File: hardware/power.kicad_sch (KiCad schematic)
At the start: 39 parts, among them J1 USB4110-GF-A, J2 B2B-PH-K-S, J3 PRPC001DAAN-RC, J4 PRPC001DAAN-RC, J5 PRPC001DAAN-RC, Q1 IRLML2246TRPBF, U1 USBLC6-2SC6, U2 BQ24074RGT, U3 TLV76733DGNR

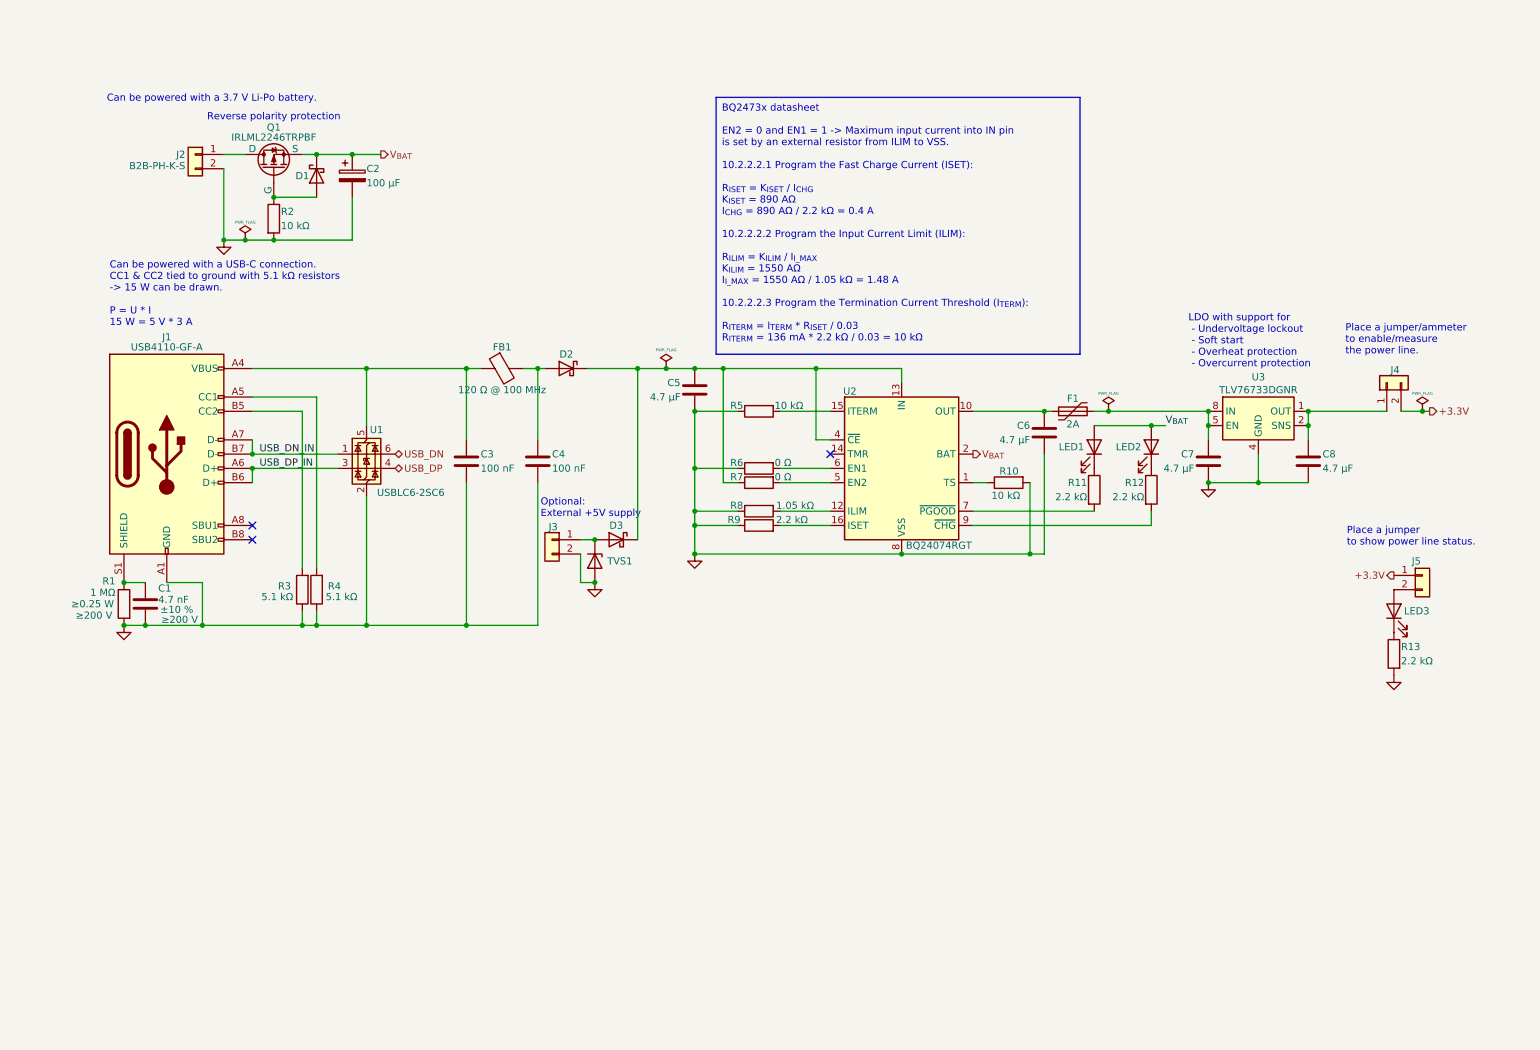
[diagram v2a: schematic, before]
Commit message: HW: Update components, change footprints to handsolder versions, finish power
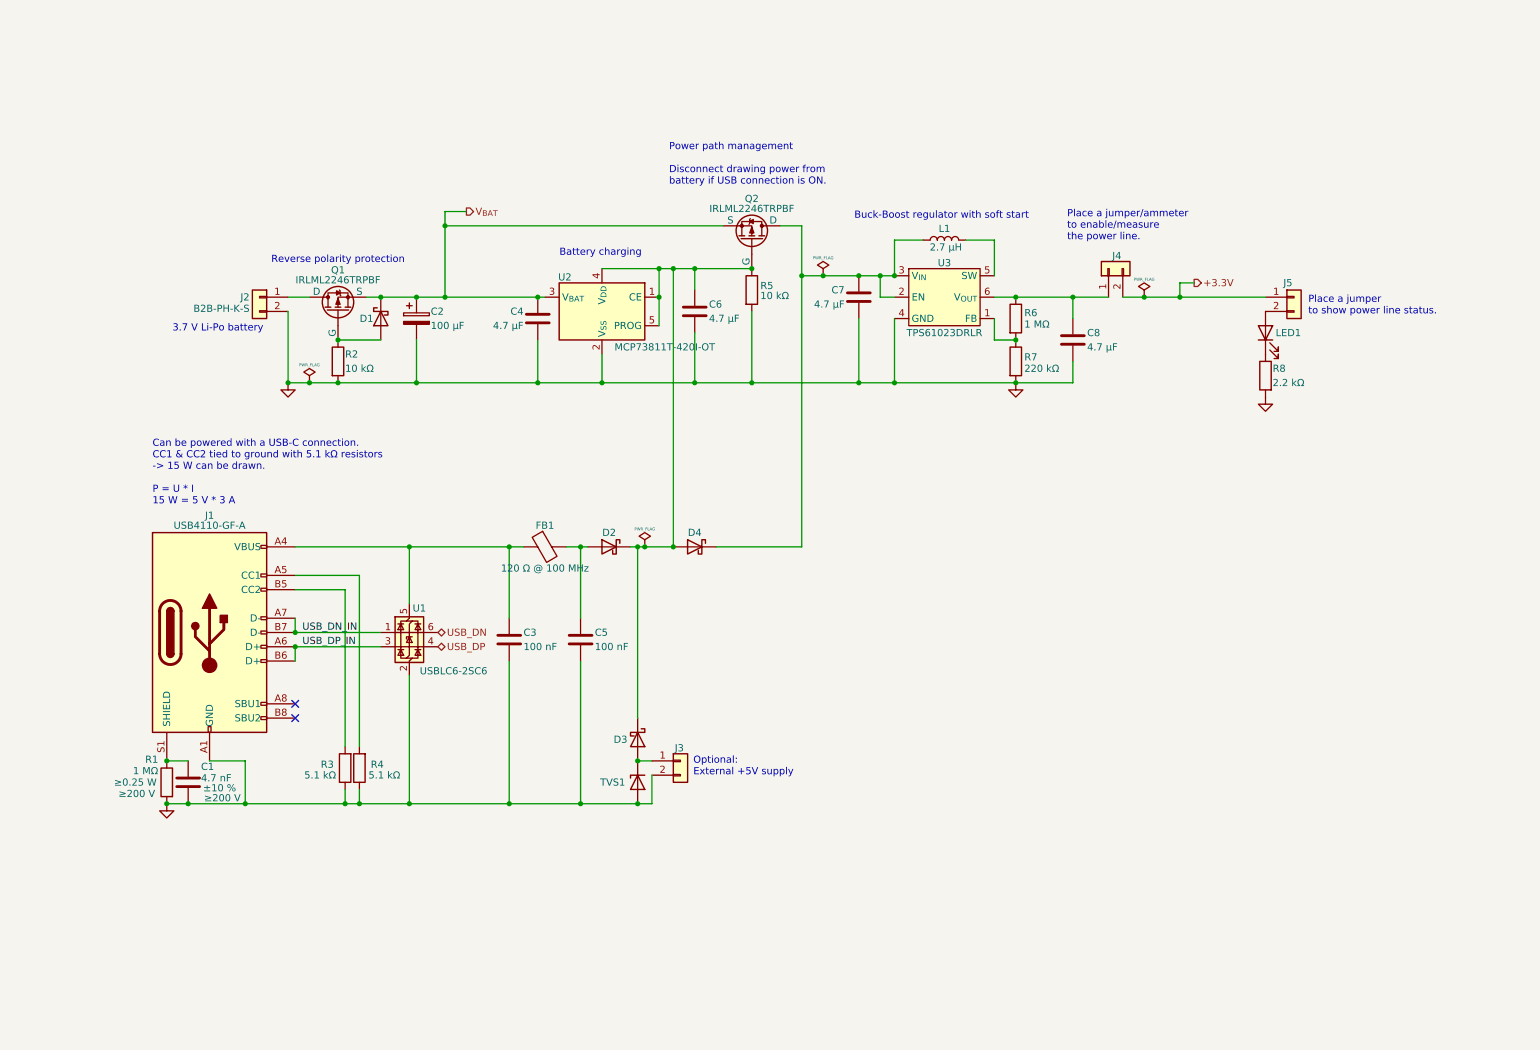
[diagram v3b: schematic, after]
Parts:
- removed C5: 4.7 µF, Capacitor_SMD:C_0603_1608Metric_Pad1.08x0.95mm_HandSolder, symbol Device:C
- removed F1: 2A, Fuse:Fuse_0805_2012Metric_Pad1.15x1.40mm_HandSolder, symbol Device:Polyfuse
- removed LED1, LED2: 150141YS73100, LED_SMD:LED_PLCC_2835_Handsoldering, symbol Device:LED
- removed R10: 10 kΩ, Resistor_SMD:R_0402_1005Metric_Pad0.72x0.64mm_HandSolder, symbol Device:R
- removed R11, R12, R9: 2.2 kΩ, Resistor_SMD:R_0402_1005Metric_Pad0.72x0.64mm_HandSolder, symbol Device:R
- removed R8: 1.05 kΩ, Resistor_SMD:R_0402_1005Metric_Pad0.72x0.64mm_HandSolder, symbol Device:R
- removed U2: BQ24074RGT, Package_DFN_QFN:VQFN-16-1EP_3x3mm_P0.5mm_EP1.68x1.68mm, symbol Battery_Management:BQ24074RGT
- removed U3: TLV76733DGNR, Package_SO:MSOP-8-1EP_3x3mm_P0.65mm_EP1.95x2.15mm, symbol TLV76733DGNR:TLV76733DGNR
- added C4: 4.7 µF, Capacitor_SMD:C_0603_1608Metric_Pad1.08x0.95mm_HandSolder, symbol Device:C
- added D4: CDBA140LL-HF, Diode_SMD:D_SMA_Handsoldering, symbol Device:D_Schottky
- added L1: 2.7 µH, Inductor_SMD:L_Bourns-SRU8028_8.0x8.0mm, symbol Device:L
- added Q2: IRLML2246TRPBF, Package_TO_SOT_SMD:SC-59_Handsoldering, symbol Simulation_SPICE:PMOS
- added U2: MCP73811T-420I-OT, Package_TO_SOT_SMD:SOT-23-5_HandSoldering, symbol Battery_Management:MCP73811T-420I-OT
- added U3: TPS61023DRLR, Package_TO_SOT_SMD:SOT-563, symbol TPS61023DRL:TPS61023DRLR
- R2, R5: Digi-Key Part Number 311-10.0KLRCT-ND -> 732-560112110020CT-ND; Manufacturer YAGEO -> Würth Elektronik; Manufacturer Part Number RC0402FR-0710KL -> 560112110020
- R3, R4: footprint Resistor_SMD:R_0402_1005Metric_Pad0.72x0.64mm_HandSolder -> Resistor_SMD:R_0603_1608Metric_Pad0.98x0.95mm_HandSolder; Digi-Key Part Number 311-5.10KLRCT-ND -> 732-560112120019CT-ND; Manufacturer YAGEO -> Würth Elektronik; Manufacturer Part Number RC0402FR-075K1L -> 560112120019
- R6: value 0 Ω -> 1 MΩ; footprint Resistor_SMD:R_0402_1005Metric_Pad0.72x0.64mm_HandSolder -> Resistor_SMD:R_1206_3216Metric_Pad1.30x1.75mm_HandSolder; Digi-Key Part Number 311-0.0JRCT-ND -> 732-560112132011CT-ND; Manufacturer YAGEO -> Würth Elektronik; Manufacturer Part Number RC0402JR-070RL -> 560112132011
- R7: value 0 Ω -> 220 kΩ; Digi-Key Part Number 311-0.0JRCT-ND -> 732-560112110217CT-ND; Manufacturer YAGEO -> Würth Elektronik; Manufacturer Part Number RC0402JR-070RL -> 560112110217
- R8: renamed from R13; Digi-Key Part Number 311-2.20KLRCT-ND -> 732-560112110087CT-ND; Manufacturer YAGEO -> Würth Elektronik; Manufacturer Part Number RC0402FR-072K2L -> 560112110087
- renumbered C4 to C5, LED3 to LED1
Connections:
- net GND: now also R5.2, R7.2, C4.2, U2.2 (V_{SS}), U3.4 (GND); no longer R5.1, R6.1
- net V_{BAT}: now also C4.1, Q2.3 (S), U2.3 (V_{BAT})
- net at C8.1, J4.1 (Pin_1): now also R6.1, U3.6 (V_{OUT})
- net at R6.2: now also R7.1, U3.1 (FB)
- net at C6.1: now also D2.1 (K), D3.1 (K), R5.1, D4.2 (A), Q2.2 (G), U2.1 (CE), U2.4 (V_{DD}), U2.5 (PROG)
- net at C7.1: now also D4.1 (K), L1.1, Q2.1 (D), U3.2 (EN), U3.3 (V_{IN})
- new net: L1.2, U3.5 (SW)
- no-connect marks 3 -> 2
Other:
- note added: "3.7 V Li-Po battery"
- note added: "Battery charging"
- note added: "Buck-Boost regulator with soft start"
- note added: "Power path management Disconnect drawing power from battery if USB connection is ON."
- note removed: "Can be powered with a 3.7 V Li-Po battery."
- note removed: "LDO with support for - Undervoltage lockout - Soft start - Overheat protection - Overcurrent protection"
- moved on the sheet: C1, C2, C3, C5, D1, D2, D3, FB1, J1, J2, J3, J4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

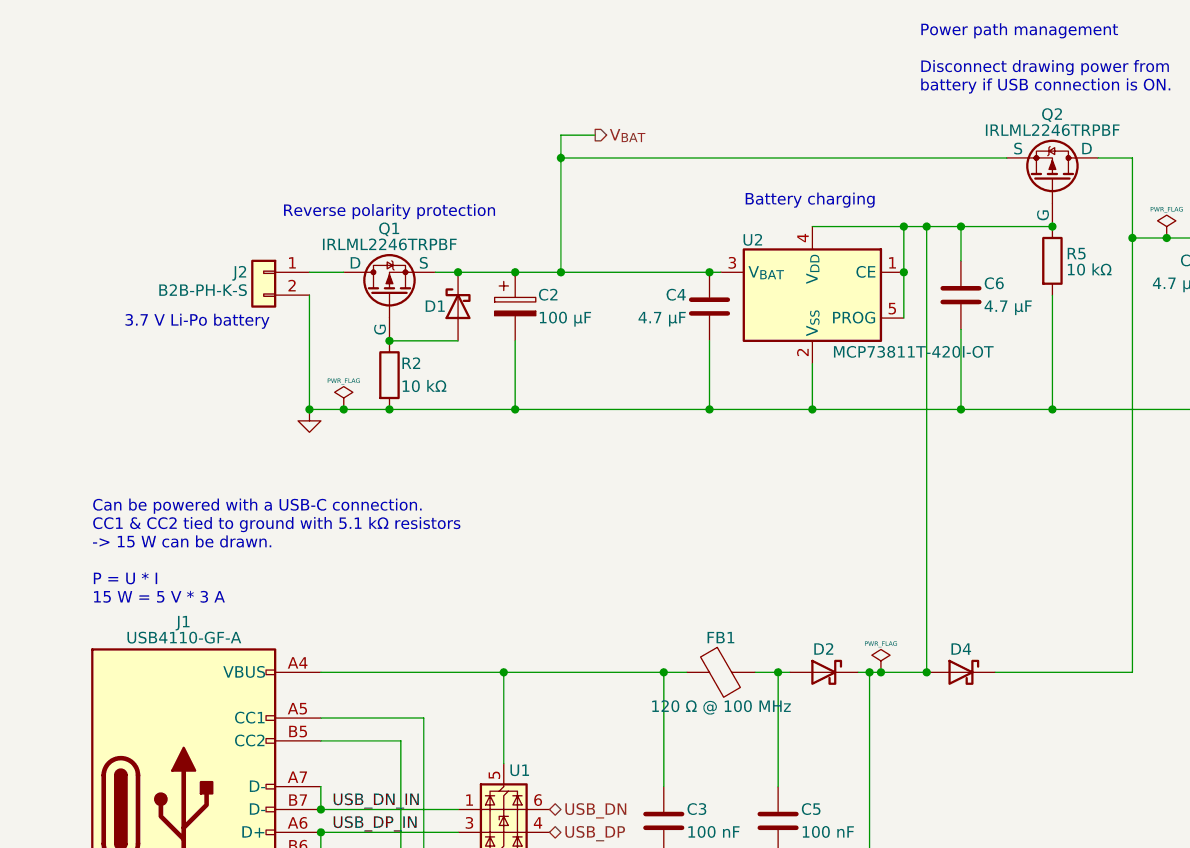
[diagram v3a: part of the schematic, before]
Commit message: HW: Add fuses to USB and battery
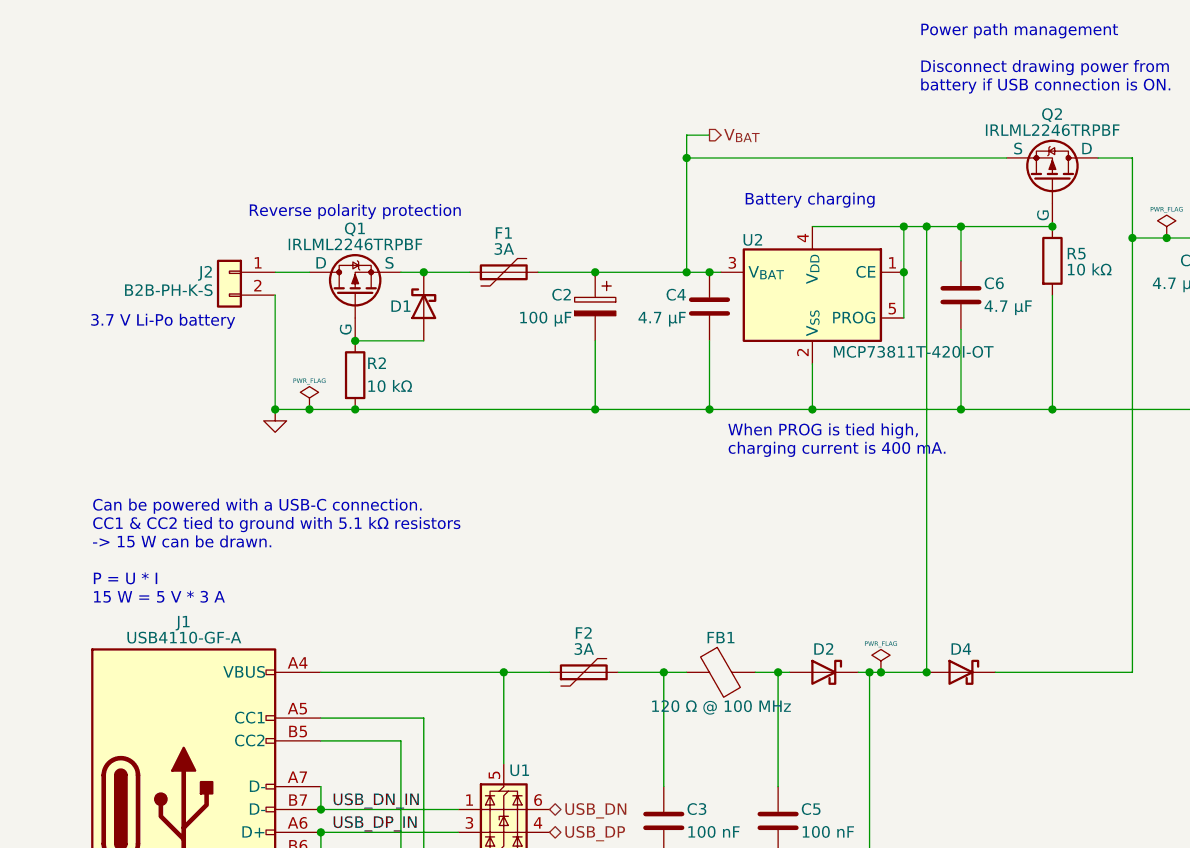
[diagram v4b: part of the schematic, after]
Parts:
- added F1, F2: 3A, Fuse:Fuse_0805_2012Metric_Pad1.15x1.40mm_HandSolder, symbol Device:Polyfuse
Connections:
- net V_{BAT}: now also F1.2; no longer D1.1 (K), Q1.3 (S)
- net at J1.A4 (VBUS), J1.A9 (VBUS), J1.B4 (VBUS)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: now also F2.1; no longer C3.1, FB1.1
- new net: D1.1 (K), F1.1, Q1.3 (S)
- new net: C3.1, F2.2, FB1.1
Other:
- note added: "When PROG is tied high, charging current is 400 mA."
- moved on the sheet: C2, D1, J2, Q1, R2

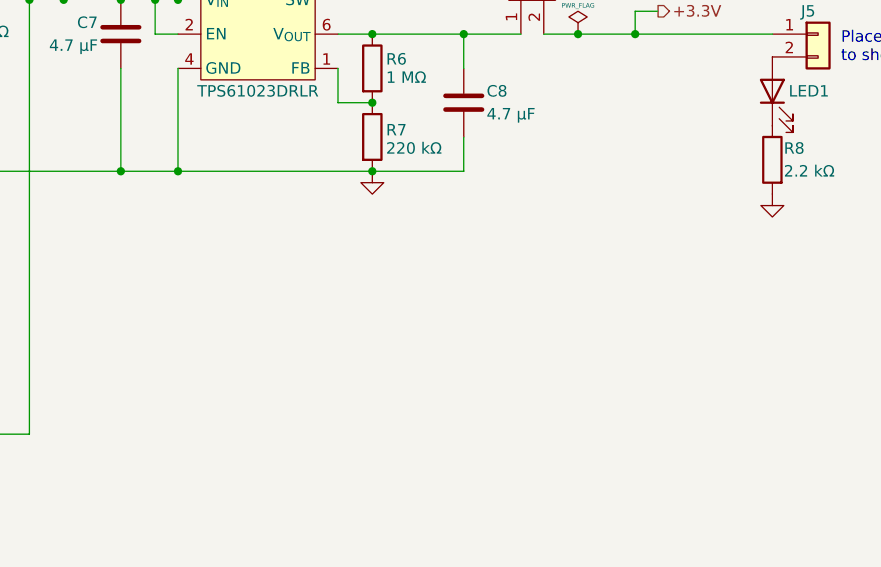
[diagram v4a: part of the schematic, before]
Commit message: HW: Add formula for FB resistors of regulator
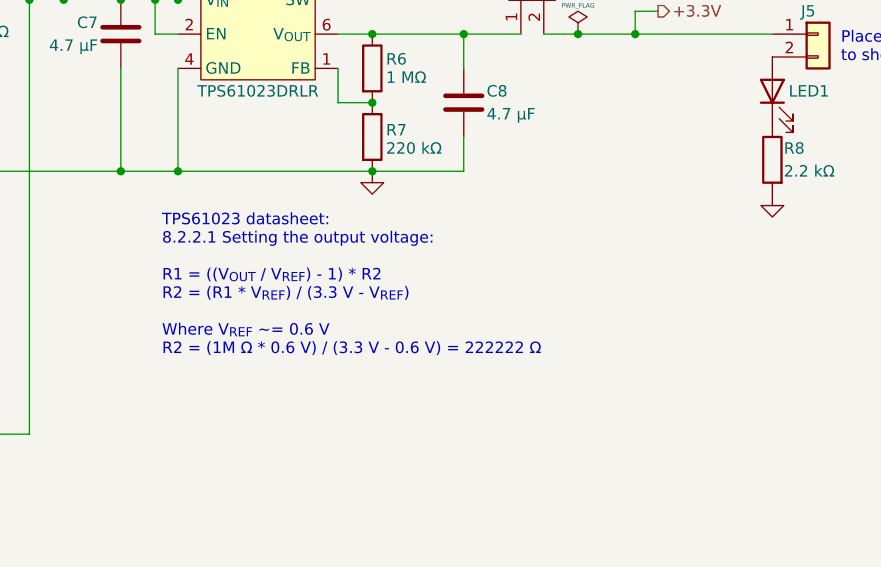
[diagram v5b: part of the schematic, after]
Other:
- note added: "TPS61023 datasheet: 8.2.2.1 Setting the output voltage: R1 = ((V_{OUT} / V_{REF}) - 1) * R2 R2 = (R1 * V_{REF}) / (3.3 V - V_{REF}) Where V_{REF} ~= 0.6 V R2 = (1M Ω * 0.6 V) / (3.3 V - 0.6 V) = 222222 Ω"
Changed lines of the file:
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@@
+		)
+	)
+	(text "TPS61023 datasheet:\n8.2.2.1 Setting the output voltage:\n\nR1 = ((V_{OUT} / V_{REF}) - 1) * R2\nR2 = (R1 * V_{REF}) / (3.3 V - V_{REF})\n\nWhere V_{REF} ~= 0.6 V\nR2 = (1M Ω * 0.6 V) / (3.3 V - 0.6 V) = 222222 Ω\n"
+		(exclude_from_sim no)
+		(at 172.212 92.71 0)
+		(effects
+			(font
+				(size 1.27 1.27)
+			)
+			(justify left)
 		)
 	)
